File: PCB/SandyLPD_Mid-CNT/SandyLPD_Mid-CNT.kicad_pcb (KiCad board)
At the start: 2 copper layers, 49.4 x 61 mm, 41 parts

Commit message: ネジ穴にスルーホールタップのアイコンを追加
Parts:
- added REF**: ICON_Through-hole_Tap, locallib:ICON_Through-hole_Tap, B.Cu at (149.1, 68.7)
- added REF**: ICON_Through-hole_Tap, locallib:ICON_Through-hole_Tap, B.Cu at (116.3, 43.7)
- added REF**: ICON_Through-hole_Tap, locallib:ICON_Through-hole_Tap, F.Cu at (149.1, 68.7)
- added REF**: ICON_Through-hole_Tap, locallib:ICON_Through-hole_Tap, F.Cu at (116.3, 43.7)
- moved REF** 3.12 mm to (112.2, 45.7)
- moved REF** 1.33 mm to (153.3, 85.5)
- moved REF** 1.19 mm to (153.7, 85.5)
- moved REF** 1.05 mm to (110.3, 45.7)

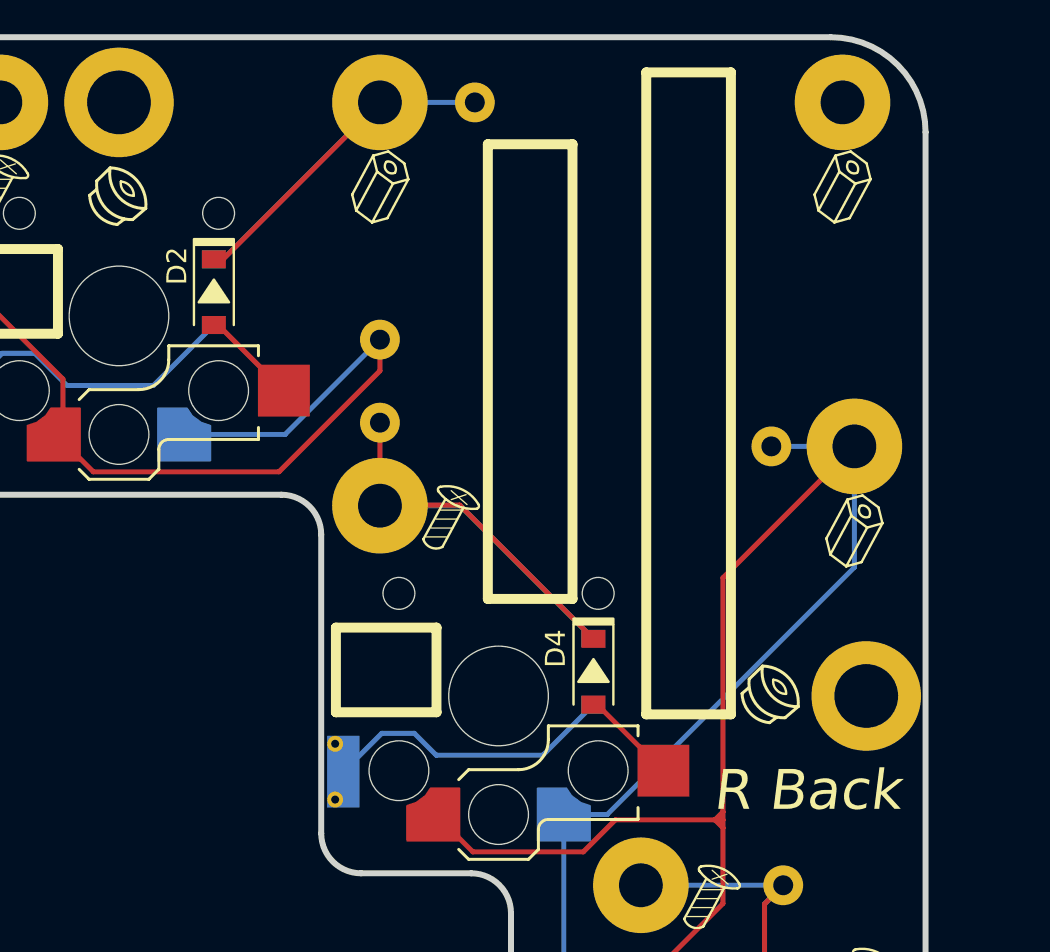
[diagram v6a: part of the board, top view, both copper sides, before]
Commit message: 間違い防止のシルク #30
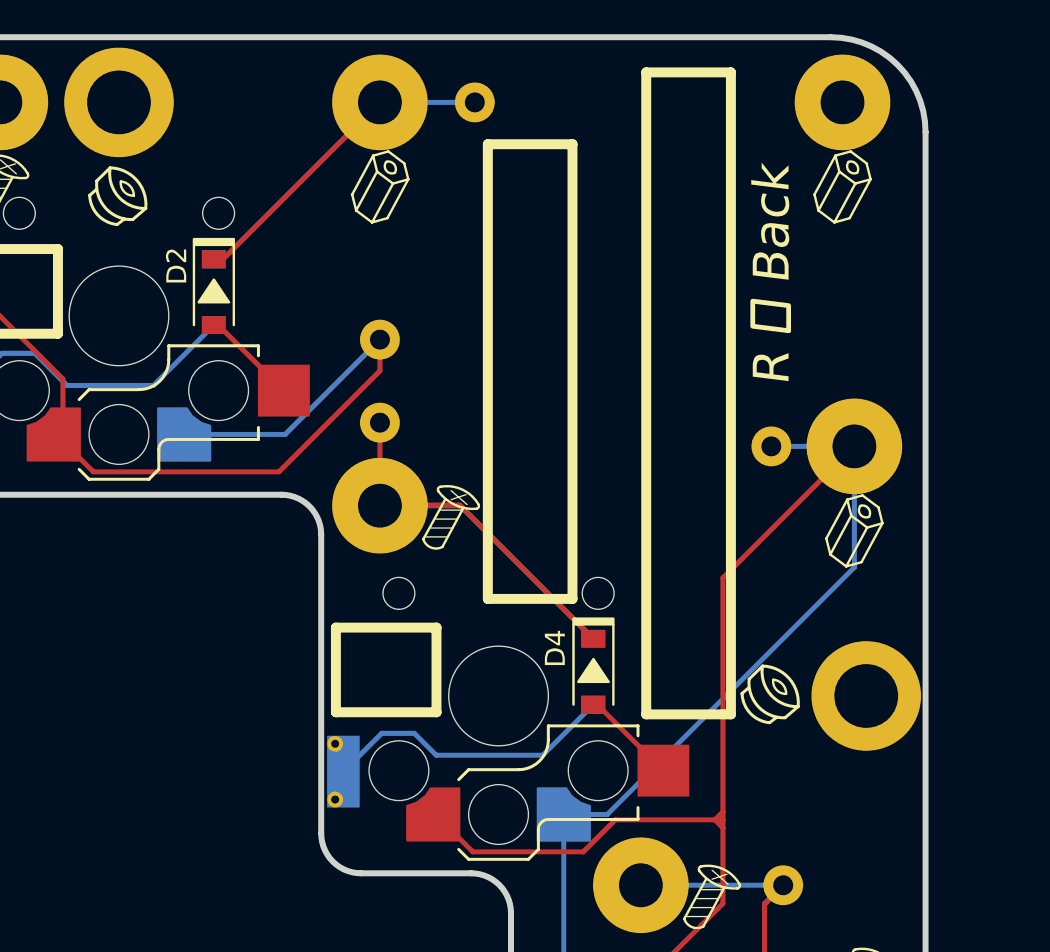
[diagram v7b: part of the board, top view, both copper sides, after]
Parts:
- turned T_C5 to 0 degrees
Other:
- board text added: "L 左 Back"
- board text added: "R 右 Back"
- board text removed: "L Back"
- board text removed: "R Back"
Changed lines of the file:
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@@
 		(fp_arc
 			(start 0.729448 -0.077979)
-			(mid 0.250509 -0.290344)
+			(mid 0.25051 -0.290344)
 			(end 0.092873 -0.789976)
 			(stroke
@@
 		(fp_arc
 			(start 0.729448 -0.077979)
-			(mid 0.250509 -0.290344)
+			(mid 0.25051 -0.290344)
 			(end 0.092873 -0.789976)
 			(stroke
@@
 			(layer "F.SilkS")
 		)
-		(group ""
-			(members "30d5ccd5-34a2-4f4d-bdec-9cd43027f3f0" "3f223cde-3b10-4852-85e9-5556bc07eb18"
-				"4c4c4600-7260-408b-b03a-5c44a166902d" "6a13ad2d-ecb3-4e6d-bab7-984d37ae1a5e"
-				"76fe9688-1813-4549-9744-3f1905e35d3c" "855f8f9e-b14e-4ee3-a3bf-8f0fcd663c15"
-				"9c6e21b8-7b4a-4011-8519-ec45bc0fc57d" "b40dad3d-4054-40c8-99ce-ba6b72ba8df4"
-				"c7a577e6-23a4-4fd2-a49c-cbcdf1cc2694" "cb7a4b12-e3dc-4430-a5eb-b4e51f9abcb4"
-			)
-		)
 	)
 	(footprint "locallib:ICON_Screw_Medium"
@@
 	(footprint "locallib:TestPoint_THTPad_D2.0mm_Drill1.0mm"
 		(layer "B.Cu")
-		(at 149.050726 56.173733 180)
+		(at 149.050726 56.173733)
 		(descr "THT pad as test Point, diameter 2.0mm, hole diameter 1.0mm")
 		(tags "test point THT pad")
 		(property "Reference" "T_C5"
-			(at 0 1.998 0)
+			(at 0 1.998 360)
 			(layer "B.SilkS")
 			(effects
@@
 		)
 		(property "Value" "Conn_01x01"
-			(at 0 -2.05 0)
+			(at 0 -2.05 360)
 			(layer "B.Fab")
 			(effects
@@
 		)
 		(property "Footprint" "locallib:TestPoint_THTPad_D2.0mm_Drill1.0mm"
-			(at 0 0 0)
+			(at 0 0 180)
 			(unlocked yes)
 			(layer "B.Fab")
@@
 		)
 		(property "Datasheet" ""
-			(at 0 0 0)
+			(at 0 0 180)
 			(unlocked yes)
 			(layer "B.Fab")
@@
 		)
 		(property "Description" ""
-			(at 0 0 0)
+			(at 0 0 180)
 			(unlocked yes)
 			(layer "B.Fab")
@@
 		)
 		(fp_text user "${REFERENCE}"
-			(at 0 2 0)
+			(at 0 2 360)
 			(layer "B.Fab")
 			(effects
@@
 		)
 		(pad "1" thru_hole circle
-			(at 0 0 180)
+			(at 0 0)
 			(size 2 2)
 			(drill 1)
@@
 			(layer "B.SilkS")
 		)
-		(group ""
-			(members "30d5ccd5-34a2-4f4d-bdec-9cd43027f3f0" "3f223cde-3b10-4852-85e9-5556bc07eb18"
-				"4c4c4600-7260-408b-b03a-5c44a166902d" "6a13ad2d-ecb3-4e6d-bab7-984d37ae1a5e"
-				"76fe9688-1813-4549-9744-3f1905e35d3c" "855f8f9e-b14e-4ee3-a3bf-8f0fcd663c15"
-				"9c6e21b8-7b4a-4011-8519-ec45bc0fc57d" "b40dad3d-4054-40c8-99ce-ba6b72ba8df4"
-				"c7a577e6-23a4-4fd2-a49c-cbcdf1cc2694" "cb7a4b12-e3dc-4430-a5eb-b4e51f9abcb4"
-			)
-		)
 	)
 	(footprint "locallib:D_SOD-123_Emphasized_Direction_Line"
@@
 		(fp_arc
 			(start 0.7 3.345415)
-			(mid 0.662237 3.758478)
+			(mid 0.662236 3.758481)
 			(end 0.272339 3.9)
 			(stroke
@@
 		(fp_arc
 			(start 0.7 3.345415)
-			(mid 0.662237 3.758478)
+			(mid 0.662236 3.758481)
 			(end 0.272339 3.9)
 			(stroke
@@
 			(layer "B.SilkS")
 		)
-		(group ""
-			(members "30d5ccd5-34a2-4f4d-bdec-9cd43027f3f0" "3f223cde-3b10-4852-85e9-5556bc07eb18"
-				"4c4c4600-7260-408b-b03a-5c44a166902d" "6a13ad2d-ecb3-4e6d-bab7-984d37ae1a5e"
-				"76fe9688-1813-4549-9744-3f1905e35d3c" "855f8f9e-b14e-4ee3-a3bf-8f0fcd663c15"
-				"9c6e21b8-7b4a-4011-8519-ec45bc0fc57d" "b40dad3d-4054-40c8-99ce-ba6b72ba8df4"
-				"c7a577e6-23a4-4fd2-a49c-cbcdf1cc2694" "cb7a4b12-e3dc-4430-a5eb-b4e51f9abcb4"
-			)
-		)
 	)
 	(footprint "locallib:TestPoint_THTPad_D2.0mm_Drill1.0mm"
@@
 		(fp_arc
 			(start 0.7 3.345415)
-			(mid 0.662236 3.758481)
+			(mid 0.662237 3.758478)
 			(end 0.272339 3.9)
 			(stroke
@@
 		(layer "F.SilkS")
 	)
-	(gr_text "L Back"
-		(at 150.836665 73.43781 0)
+	(gr_text "L 左 Back"
+		(at 149.183435 47.50028 90)
 		(layer "B.SilkS" knockout)
 		(effects
 			(font
-				(size 2 2)
-				(thickness 0.3)
+				(size 1.8 1.8)
+				(thickness 0.24)
 				(italic yes)
 			)
@@
 		)
 	)
-	(gr_text "R Back"
-		(at 150.836665 73.43781 0)
+	(gr_text "R 右 Back"
+		(at 149.083435 47.60028 90)
 		(layer "F.SilkS" knockout)
 		(effects
 			(font
-				(size 2 2)
-				(thickness 0.3)
+				(size 1.8 1.8)
+				(thickness 0.24)
 				(italic yes)
 			)

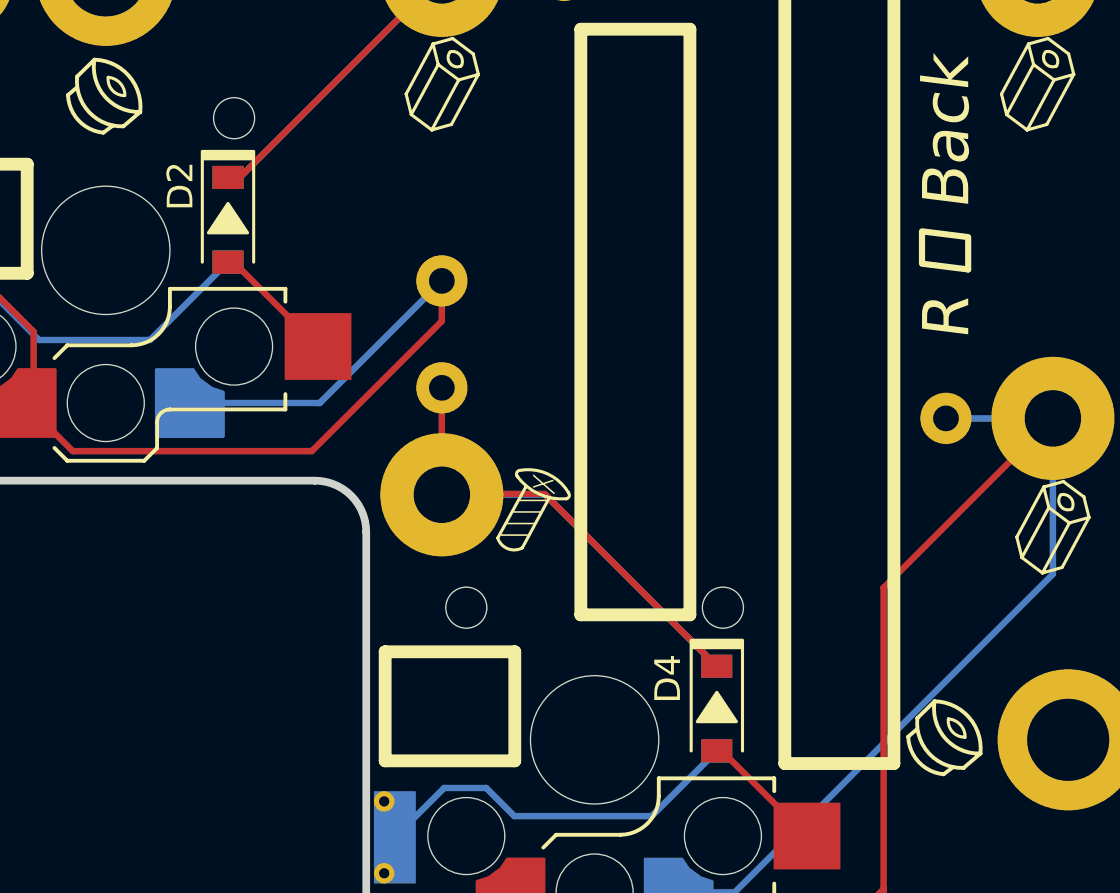
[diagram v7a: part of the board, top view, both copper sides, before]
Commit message: ダイオードの番号を調整
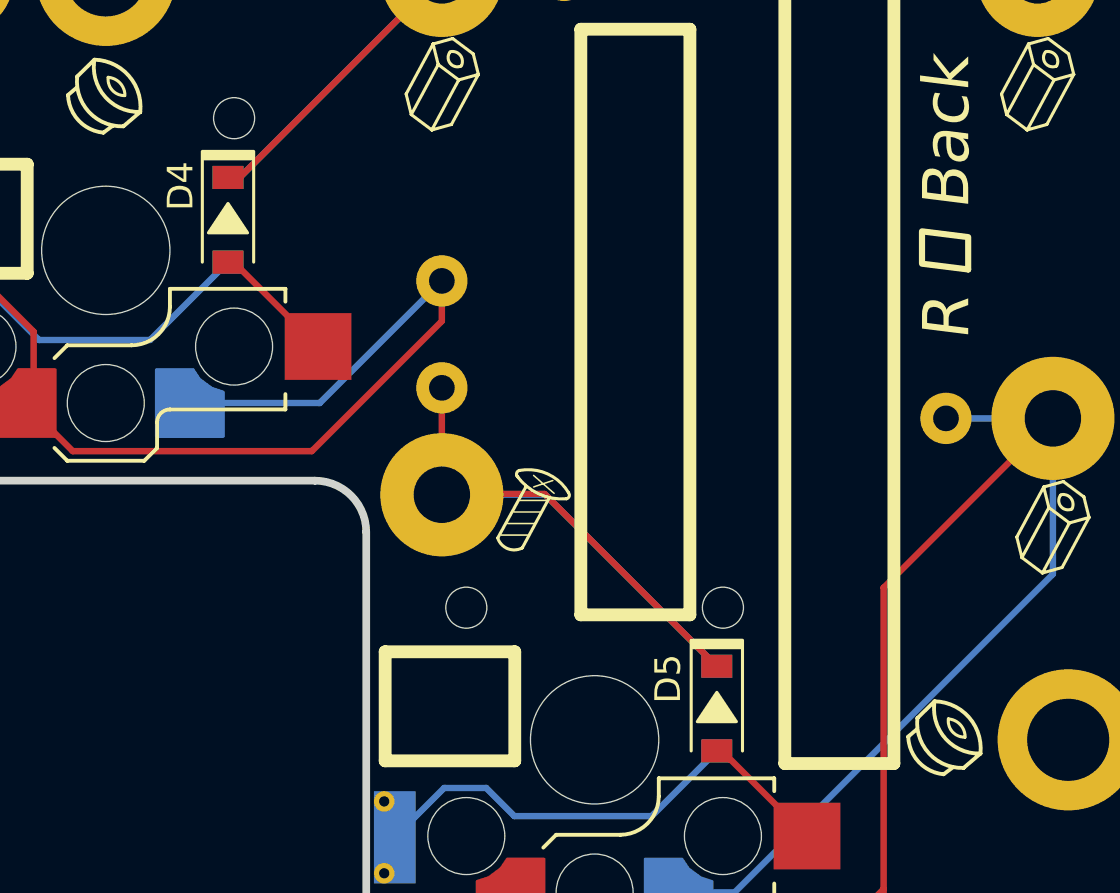
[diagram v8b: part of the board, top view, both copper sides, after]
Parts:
- renumbered D3 to D2, D5 to D3, D2 to D4, D4 to D5, T_R1 to T_R0, T_R2 to T_R1, T_R3 to T_R2
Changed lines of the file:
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@@
 			(layers "*.Cu" "*.Mask")
 			(remove_unused_layers no)
-			(net 1 "Net-(D3-A)")
+			(net 6 "Net-(D2-A)")
 			(pinfunction "2")
 			(pintype "passive")
@@
 			(layers "*.Cu" "*.Mask")
 			(remove_unused_layers no)
-			(net 1 "Net-(D3-A)")
+			(net 6 "Net-(D2-A)")
 			(pinfunction "2")
 			(pintype "passive")
@@
 			(size 1.625 3.6)
 			(layers "B.Cu" "B.Paste" "B.Mask")
-			(net 1 "Net-(D3-A)")
+			(net 6 "Net-(D2-A)")
 			(pinfunction "2")
 			(pintype "passive")
@@
 		(descr "SOD-123")
 		(tags "SOD-123")
-		(property "Reference" "D2"
+		(property "Reference" "D4"
 			(at -1.315634 1.85008 90)
 			(layer "F.SilkS")
@@
 			(size 0.9 1.2)
 			(layers "F.Cu" "F.Paste" "F.Mask")
-			(net 6 "Net-(D2-A)")
+			(net 2 "Net-(D4-A)")
 			(pinfunction "A")
 			(pintype "passive")
@@
 		(fp_arc
 			(start 0.729448 -0.077979)
-			(mid 0.25051 -0.290344)
+			(mid 0.250512 -0.290345)
 			(end 0.092873 -0.789976)
 			(stroke
@@
 		(descr "SOD-123")
 		(tags "SOD-123")
-		(property "Reference" "D4"
+		(property "Reference" "D5"
 			(at -1.16565 1.900096 90)
 			(layer "F.SilkS")
@@
 			(size 0.9 1.2)
 			(layers "F.Cu" "F.Paste" "F.Mask")
-			(net 2 "Net-(D4-A)")
+			(net 8 "Net-(D5-A)")
 			(pinfunction "A")
 			(pintype "passive")
@@
 			(layers "*.Cu" "*.Mask")
 			(remove_unused_layers no)
-			(net 8 "Net-(D5-A)")
+			(net 1 "Net-(D3-A)")
 			(pinfunction "2")
 			(pintype "passive")
@@
 			(layers "*.Cu" "*.Mask")
 			(remove_unused_layers no)
-			(net 8 "Net-(D5-A)")
+			(net 1 "Net-(D3-A)")
 			(pinfunction "2")
 			(pintype "passive")
@@
 			(size 1.625 3.6)
 			(layers "B.Cu" "B.Paste" "B.Mask")
-			(net 8 "Net-(D5-A)")
+			(net 1 "Net-(D3-A)")
 			(pinfunction "2")
 			(pintype "passive")
@@
 		(fp_arc
 			(start 0.729448 -0.077979)
-			(mid 0.25051 -0.290344)
+			(mid 0.250512 -0.290345)
 			(end 0.092873 -0.789976)
 			(stroke
@@
 		(tags "test point THT pad")
 		(property "Reference" "T_C5"
-			(at 0 1.998 360)
+			(at 0 1.998 0)
 			(layer "B.SilkS")
 			(effects
@@
 		)
 		(property "Value" "Conn_01x01"
-			(at 0 -2.05 360)
+			(at 0 -2.05 0)
 			(layer "B.Fab")
 			(effects
@@
 		)
 		(fp_text user "${REFERENCE}"
-			(at 0 2 360)
+			(at 0 2 0)
 			(layer "B.Fab")
 			(effects
@@
 			(size 2.6 2.6)
 			(layers "F.Cu" "F.Paste" "F.Mask")
-			(net 2 "Net-(D4-A)")
+			(net 8 "Net-(D5-A)")
 			(pinfunction "2")
 			(pintype "passive")
@@
 		(descr "SOD-123")
 		(tags "SOD-123")
-		(property "Reference" "D5"
-			(at -1.190585 1.785939 90)
+		(property "Reference" "D3"
+			(at -1.334375 1.785939 90)
 			(layer "B.SilkS")
 			(effects
@@
 			(size 0.9 1.2)
 			(layers "B.Cu" "B.Paste" "B.Mask")
-			(net 8 "Net-(D5-A)")
+			(net 1 "Net-(D3-A)")
 			(pinfunction "A")
 			(pintype "passive")
@@
 		(descr "SOD-123")
 		(tags "SOD-123")
-		(property "Reference" "D3"
+		(property "Reference" "D2"
 			(at -1.165625 1.9 90)
 			(layer "B.SilkS")
@@
 			(size 0.9 1.2)
 			(layers "B.Cu" "B.Paste" "B.Mask")
-			(net 1 "Net-(D3-A)")
+			(net 6 "Net-(D2-A)")
 			(pinfunction "A")
 			(pintype "passive")
@@
 		(fp_arc
 			(start 0.7 3.345415)
-			(mid 0.662236 3.758481)
+			(mid 0.662237 3.758478)
 			(end 0.272339 3.9)
 			(stroke
@@
 		(fp_arc
 			(start 0.7 3.345415)
-			(mid 0.662236 3.758481)
+			(mid 0.662237 3.758478)
 			(end 0.272339 3.9)
 			(stroke
@@
 		(descr "THT pad as test Point, diameter 2.0mm, hole diameter 1.0mm")
 		(tags "test point THT pad")
-		(property "Reference" "T_R2"
+		(property "Reference" "T_R1"
 			(at -3.571878 0.735923 0)
 			(layer "B.SilkS")
@@
 		(descr "THT pad as test Point, diameter 2.0mm, hole diameter 1.0mm")
 		(tags "test point THT pad")
-		(property "Reference" "T_R1"
+		(property "Reference" "T_R0"
 			(at 0 1.998 0)
 			(layer "B.SilkS")
@@
 			(size 2.6 2.6)
 			(layers "F.Cu" "F.Paste" "F.Mask")
-			(net 6 "Net-(D2-A)")
+			(net 2 "Net-(D4-A)")
 			(pinfunction "2")
 			(pintype "passive")
@@
 		(descr "THT pad as test Point, diameter 2.0mm, hole diameter 1.0mm")
 		(tags "test point THT pad")
-		(property "Reference" "T_R3"
+		(property "Reference" "T_R2"
 			(at -0.025 -2.08125 0)
 			(layer "B.SilkS")
@@
 		(fp_arc
 			(start 0.7 3.345415)
-			(mid 0.662237 3.758478)
+			(mid 0.662236 3.758481)
 			(end 0.272339 3.9)
 			(stroke
@@
 	)
 	(segment
-		(start 140.120935 69.134655)
-		(end 137.58192 71.67367)
+		(start 137.095935 91.52528)
+		(end 141.120935 95.55028)
 		(width 0.25)
 		(layer "B.Cu")
@@
 	)
 	(segment
-		(start 137.58192 71.67367)
-		(end 132.233435 71.67367)
+		(start 149.589685 95.55028)
+		(end 151.758435 93.38153)
 		(width 0.25)
 		(layer "B.Cu")
@@
 	)
 	(segment
-		(start 131.135085 70.57532)
-		(end 129.495935 70.57532)
+		(start 141.120935 95.55028)
+		(end 149.589685 95.55028)
 		(width 0.25)
 		(layer "B.Cu")
@@
 	)
 	(segment
-		(start 132.233435 71.67367)
-		(end 131.135085 70.57532)
+		(start 151.758435 90.297051)
+		(end 149.646039 88.184655)
 		(width 0.25)
 		(layer "B.Cu")
@@
 	)
 	(segment
-		(start 129.495935 70.57532)
-		(end 127.570935 72.50032)
+		(start 151.758435 93.38153)
+		(end 151.758435 90.297051)
 		(width 0.25)
 		(layer "B.Cu")
@@
 	)
 	(segment
-		(start 140.121031 69.13468)
-		(end 140.317795 69.13468)
+		(start 121.071015 50.084664)
+		(end 121.292819 50.084664)
 		(width 0.25)
 		(layer "F.Cu")
@@
 	)
 	(segment
-		(start 140.317795 69.13468)
-		(end 143.633435 72.45032)
+		(start 121.292819 50.084664)
+		(end 124.583435 53.37528)
 		(width 0.25)
 		(layer "F.Cu")
@@
 	)
 	(segment
-		(start 121.071015 50.084664)
-		(end 121.292819 50.084664)
+		(start 140.120935 69.134655)
+		(end 137.58192 71.67367)
 		(width 0.25)
-		(layer "F.Cu")
+		(layer "B.Cu")
 		(net 6)
 	)
 	(segment
-		(start 121.292819 50.084664)
-		(end 124.583435 53.37528)
+		(start 137.58192 71.67367)
+		(end 132.233435 71.67367)
 		(width 0.25)
-		(layer "F.Cu")
+		(layer "B.Cu")
+		(net 6)
+	)
+	(segment
+		(start 131.135085 70.57532)
+		(end 129.495935 70.57532)
+		(width 0.25)
+		(layer "B.Cu")
+		(net 6)
+	)
+	(segment
+		(start 132.233435 71.67367)
+		(end 131.135085 70.57532)
+		(width 0.25)
+		(layer "B.Cu")
+		(net 6)
+	)
+	(segment
+		(start 129.495935 70.57532)
+		(end 127.570935 72.50032)
+		(width 0.25)
+		(layer "B.Cu")
 		(net 6)
 	)
@@
 	)
 	(segment
-		(start 137.095935 91.52528)
-		(end 141.120935 95.55028)
-		(width 0.25)
-		(layer "B.Cu")
-		(net 8)
-	)
-	(segment
-		(start 149.589685 95.55028)
-		(end 151.758435 93.38153)
-		(width 0.25)
-		(layer "B.Cu")
-		(net 8)
-	)
-	(segment
-		(start 141.120935 95.55028)
-		(end 149.589685 95.55028)
-		(width 0.25)
-		(layer "B.Cu")
-		(net 8)
-	)
-	(segment
-		(start 151.758435 90.297051)
-		(end 149.646039 88.184655)
+		(start 140.121031 69.13468)
+		(end 140.317795 69.13468)
 		(width 0.25)
-		(layer "B.Cu")
+		(layer "F.Cu")
 		(net 8)
 	)
 	(segment
-		(start 151.758435 93.38153)
-		(end 151.758435 90.297051)
+		(start 140.317795 69.13468)
+		(end 143.633435 72.45032)
 		(width 0.25)
-		(layer "B.Cu")
+		(layer "F.Cu")
 		(net 8)
 	)
